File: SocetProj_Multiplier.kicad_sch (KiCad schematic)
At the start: 23 parts, among them J1 Barrel_Jack, U1 74LS283, U2 74LS283, U4 74LS86, U5 74LS86

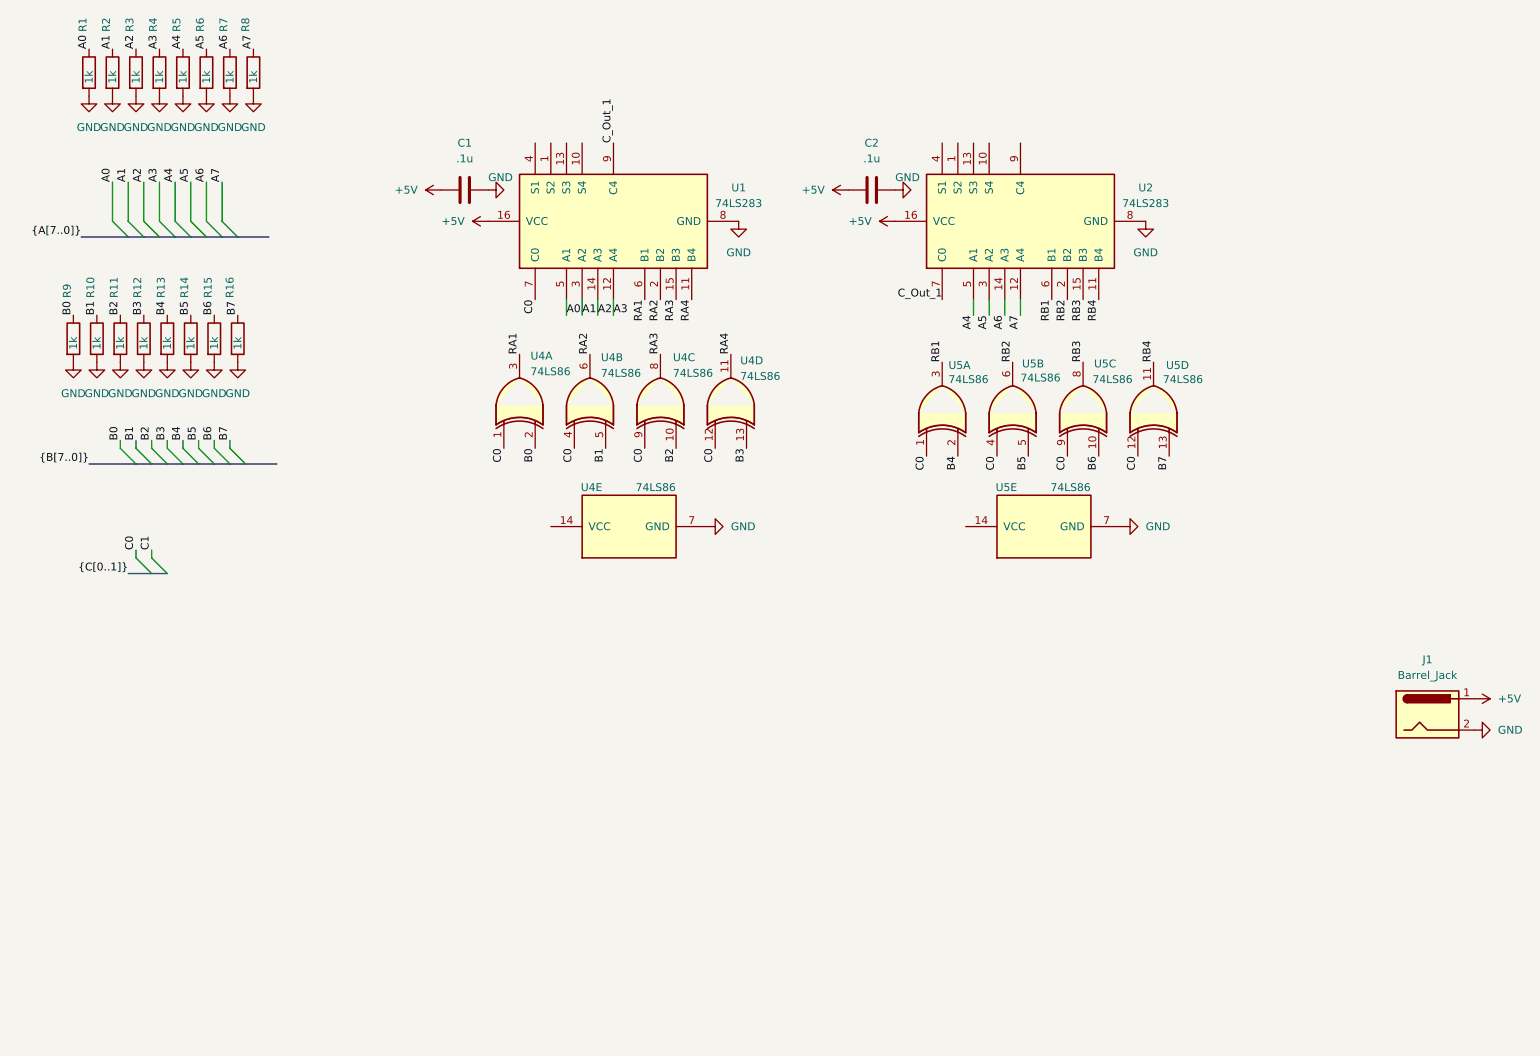
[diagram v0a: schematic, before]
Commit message: Begun Dadda logic
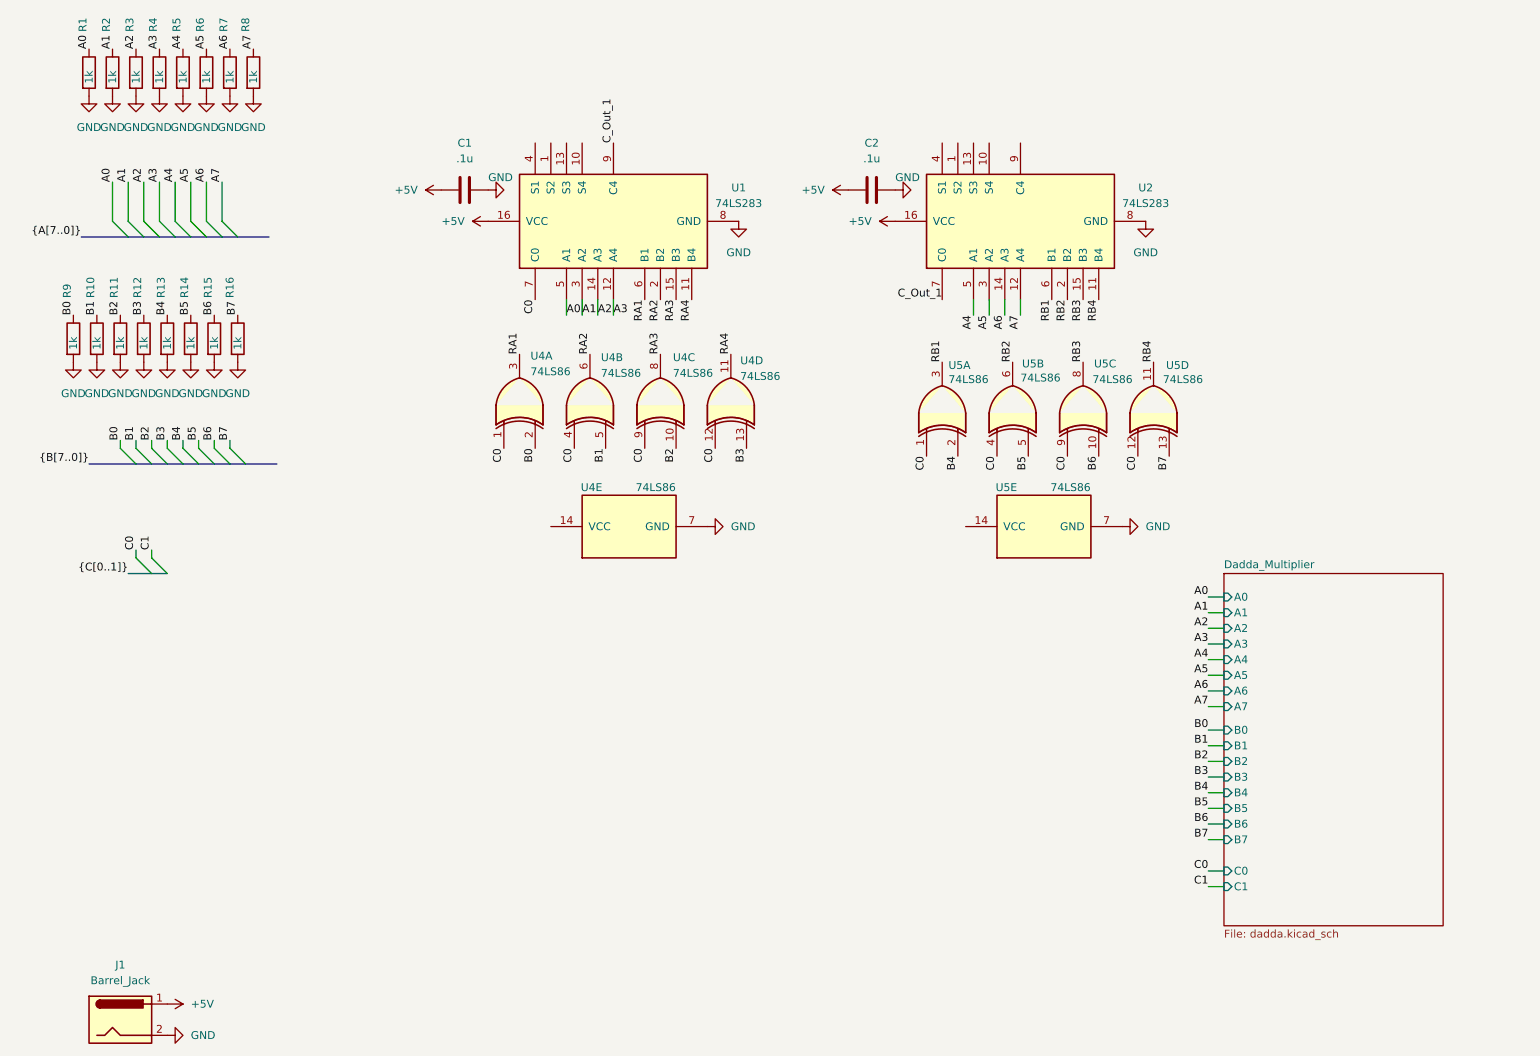
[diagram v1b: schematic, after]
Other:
- added sheet Dadda_Multiplier (dadda.kicad_sch)
- moved on the sheet: J1

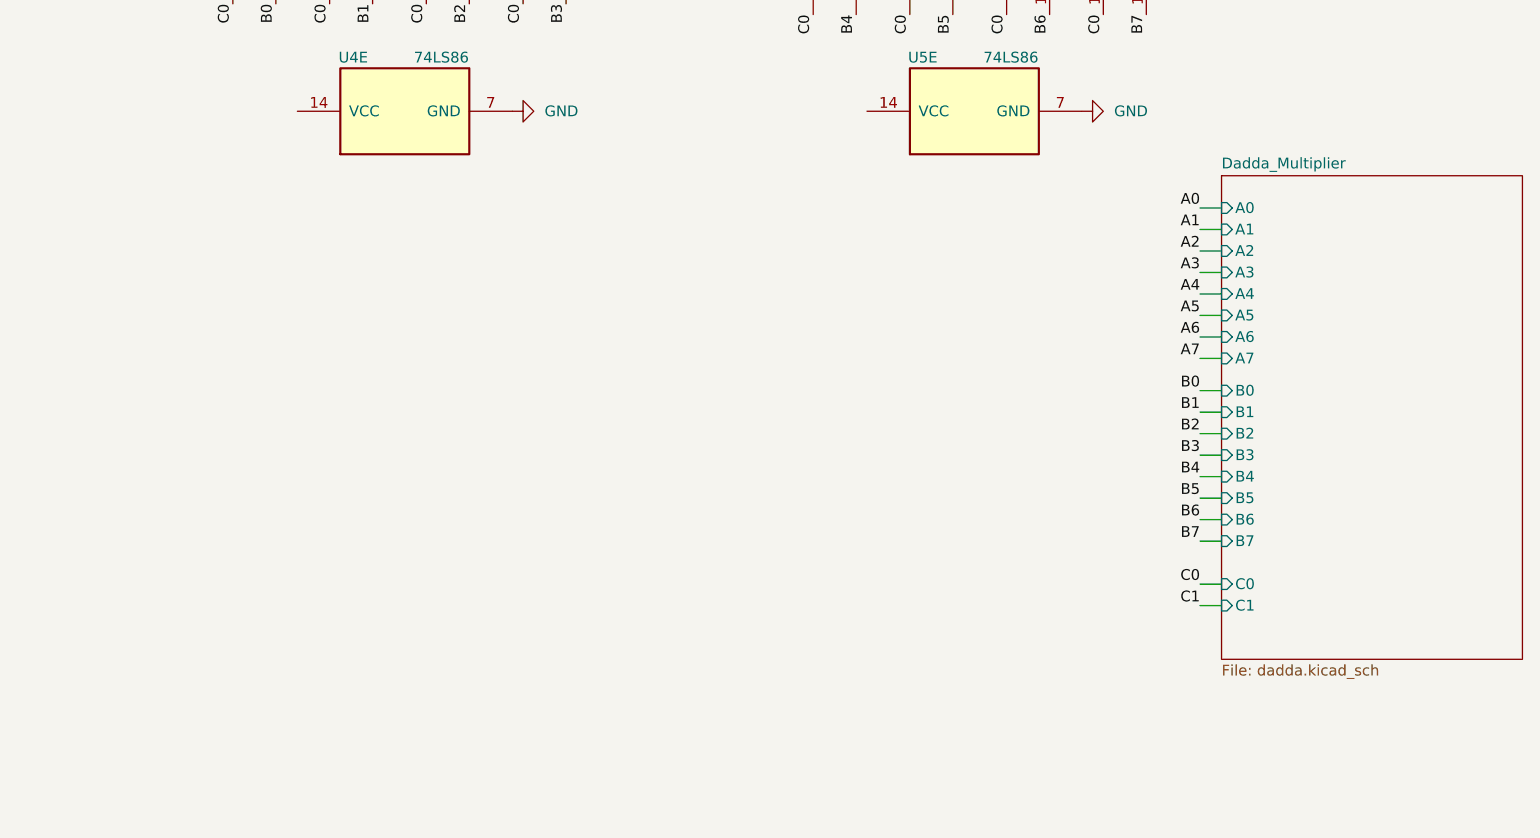
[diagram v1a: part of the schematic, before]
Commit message: Added hierarchal partial product outputs, need to complete treemultiplier
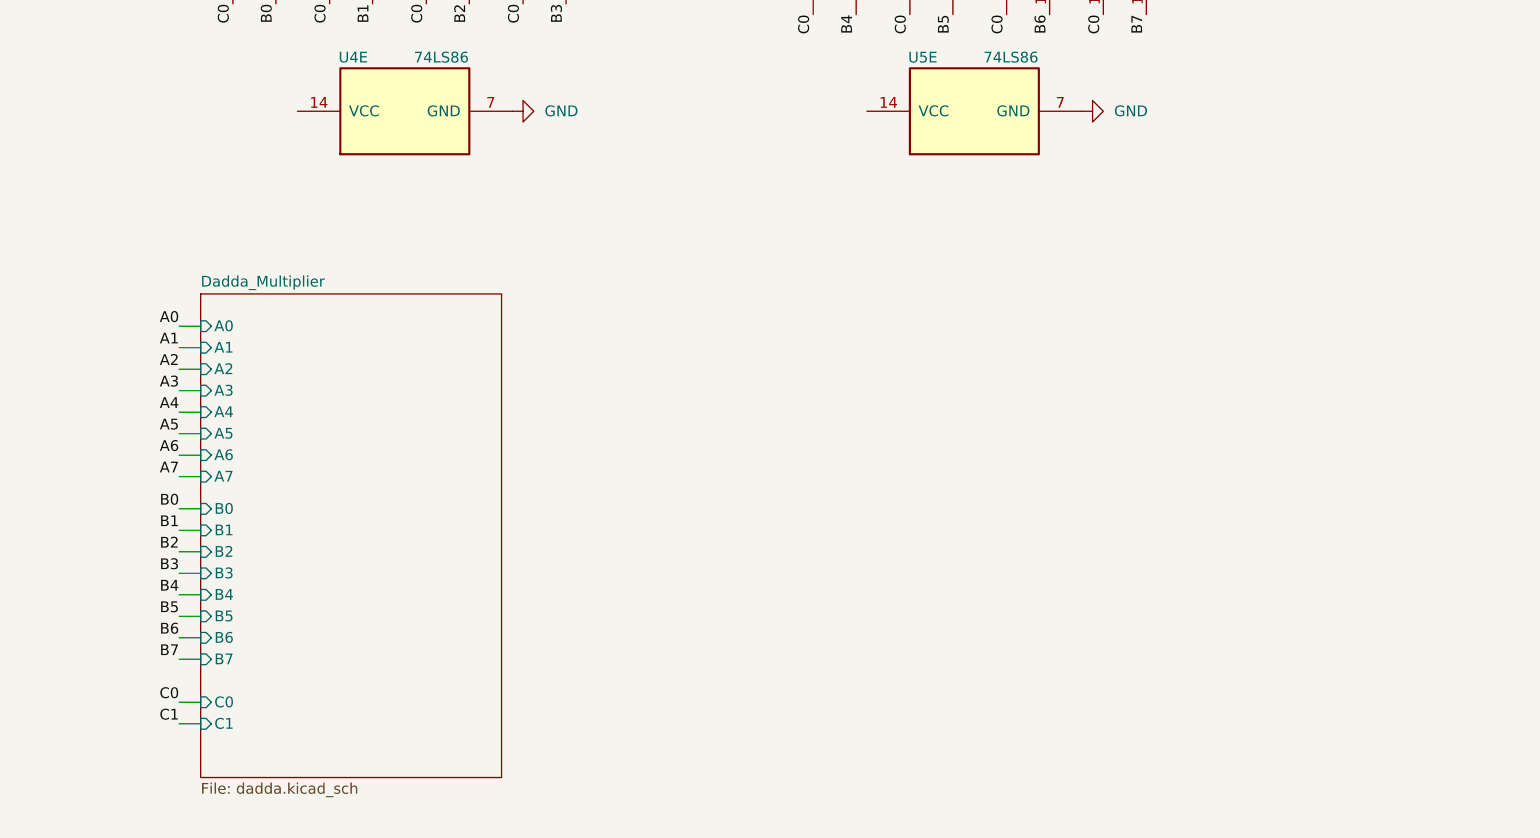
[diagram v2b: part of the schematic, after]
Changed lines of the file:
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@@
 	(wire
 		(pts
-			(xy 213.36 116.84) (xy 215.9 116.84)
+			(xy 92.71 130.81) (xy 95.25 130.81)
 		)
 		(stroke
@@
 	(wire
 		(pts
-			(xy 213.36 121.92) (xy 215.9 121.92)
+			(xy 92.71 135.89) (xy 95.25 135.89)
 		)
 		(stroke
@@
 	(wire
 		(pts
-			(xy 213.36 127) (xy 215.9 127)
+			(xy 92.71 140.97) (xy 95.25 140.97)
 		)
 		(stroke
@@
 	(wire
 		(pts
-			(xy 213.36 124.46) (xy 215.9 124.46)
+			(xy 92.71 138.43) (xy 95.25 138.43)
 		)
 		(stroke
@@
 	(wire
 		(pts
-			(xy 213.36 135.89) (xy 215.9 135.89)
+			(xy 92.71 149.86) (xy 95.25 149.86)
 		)
 		(stroke
@@
 	(wire
 		(pts
-			(xy 213.36 114.3) (xy 215.9 114.3)
+			(xy 92.71 128.27) (xy 95.25 128.27)
 		)
 		(stroke
@@
 	(wire
 		(pts
-			(xy 213.36 153.67) (xy 215.9 153.67)
+			(xy 92.71 167.64) (xy 95.25 167.64)
 		)
 		(stroke
@@
 	(wire
 		(pts
-			(xy 213.36 119.38) (xy 215.9 119.38)
+			(xy 92.71 133.35) (xy 95.25 133.35)
 		)
 		(stroke
@@
 	(wire
 		(pts
-			(xy 213.36 111.76) (xy 215.9 111.76)
+			(xy 92.71 125.73) (xy 95.25 125.73)
 		)
 		(stroke
@@
 	(wire
 		(pts
-			(xy 213.36 133.35) (xy 215.9 133.35)
+			(xy 92.71 147.32) (xy 95.25 147.32)
 		)
 		(stroke
@@
 	(wire
 		(pts
-			(xy 213.36 156.21) (xy 215.9 156.21)
+			(xy 92.71 170.18) (xy 95.25 170.18)
 		)
 		(stroke
@@
 	(wire
 		(pts
-			(xy 213.36 138.43) (xy 215.9 138.43)
+			(xy 92.71 152.4) (xy 95.25 152.4)
 		)
 		(stroke
@@
 	(wire
 		(pts
-			(xy 213.36 109.22) (xy 215.9 109.22)
+			(xy 92.71 123.19) (xy 95.25 123.19)
 		)
 		(stroke
@@
 	(wire
 		(pts
-			(xy 213.36 146.05) (xy 215.9 146.05)
+			(xy 92.71 160.02) (xy 95.25 160.02)
 		)
 		(stroke
@@
 	(wire
 		(pts
-			(xy 213.36 148.59) (xy 215.9 148.59)
+			(xy 92.71 162.56) (xy 95.25 162.56)
 		)
 		(stroke
@@
 	(wire
 		(pts
-			(xy 213.36 143.51) (xy 215.9 143.51)
+			(xy 92.71 157.48) (xy 95.25 157.48)
 		)
 		(stroke
@@
 	(wire
 		(pts
-			(xy 213.36 130.81) (xy 215.9 130.81)
+			(xy 92.71 144.78) (xy 95.25 144.78)
 		)
 		(stroke
@@
 	(wire
 		(pts
-			(xy 213.36 140.97) (xy 215.9 140.97)
+			(xy 92.71 154.94) (xy 95.25 154.94)
 		)
 		(stroke
@@
 	)
 	(label "B0"
-		(at 213.36 130.81 180)
+		(at 92.71 144.78 180)
 		(effects
 			(font
@@
 	)
 	(label "A6"
-		(at 213.36 124.46 180)
+		(at 92.71 138.43 180)
 		(effects
 			(font
@@
 	)
 	(label "A7"
-		(at 213.36 127 180)
+		(at 92.71 140.97 180)
 		(effects
 			(font
@@
 	)
 	(label "A2"
-		(at 213.36 114.3 180)
+		(at 92.71 128.27 180)
 		(effects
 			(font
@@
 	)
 	(label "B1"
-		(at 213.36 133.35 180)
+		(at 92.71 147.32 180)
 		(effects
 			(font
@@
 	)
 	(label "A1"
-		(at 213.36 111.76 180)
+		(at 92.71 125.73 180)
 		(effects
 			(font
@@
 	)
 	(label "B2"
-		(at 213.36 135.89 180)
+		(at 92.71 149.86 180)
 		(effects
 			(font
@@
 	)
 	(label "A0"
-		(at 213.36 109.22 180)
+		(at 92.71 123.19 180)
 		(effects
 			(font
@@
 	)
 	(label "B7"
-		(at 213.36 148.59 180)
+		(at 92.71 162.56 180)
 		(effects
 			(font
@@
 	)
 	(label "B6"
-		(at 213.36 146.05 180)
+		(at 92.71 160.02 180)
 		(effects
 			(font
@@
 	)
 	(label "B5"
-		(at 213.36 143.51 180)
+		(at 92.71 157.48 180)
 		(effects
 			(font
@@
 	)
 	(label "A4"
-		(at 213.36 119.38 180)
+		(at 92.71 133.35 180)
 		(effects
 			(font
@@
 	)
 	(label "C0"
-		(at 213.36 153.67 180)
+		(at 92.71 167.64 180)
 		(effects
 			(font
@@
 	)
 	(label "B4"
-		(at 213.36 140.97 180)
+		(at 92.71 154.94 180)
 		(effects
 			(font
@@
 	)
 	(label "B3"
-		(at 213.36 138.43 180)
+		(at 92.71 152.4 180)
 		(effects
 			(font
@@
 	)
 	(label "C1"
-		(at 213.36 156.21 180)
+		(at 92.71 170.18 180)
 		(effects
 			(font
@@
 	)
 	(label "A3"
-		(at 213.36 116.84 180)
+		(at 92.71 130.81 180)
 		(effects
 			(font
@@
 	)
 	(label "A5"
-		(at 213.36 121.92 180)
+		(at 92.71 135.89 180)
 		(effects
 			(font
@@
 	)
 	(sheet
-		(at 215.9 105.41)
+		(at 95.25 119.38)
 		(size 35.56 57.15)
 		(exclude_from_sim no)
@@
 		)
 		(property "Sheetname" "Dadda_Multiplier"
-			(at 215.9 104.6984 0)
+			(at 95.25 118.6684 0)
 			(effects
 				(font
@@
 		)
 		(property "Sheetfile" "dadda.kicad_sch"
-			(at 215.9 163.1446 0)
+			(at 95.25 177.1146 0)
 			(effects
 				(font
@@
 		)
 		(pin "A0" input
-			(at 215.9 109.22 180)
+			(at 95.25 123.19 180)
 			(effects
 				(font
@@
 		)
 		(pin "A1" input
-			(at 215.9 111.76 180)
+			(at 95.25 125.73 180)
 			(effects
 				(font
@@
 		)
 		(pin "A2" input
-			(at 215.9 114.3 180)
+			(at 95.25 128.27 180)
 			(effects
 				(font
@@
 		)
 		(pin "A3" input
-			(at 215.9 116.84 180)
+			(at 95.25 130.81 180)
 			(effects
 				(font
@@
 		)
 		(pin "A4" input
-			(at 215.9 119.38 180)
+			(at 95.25 133.35 180)
 			(effects
 				(font
@@
 		)
 		(pin "A5" input
-			(at 215.9 121.92 180)
+			(at 95.25 135.89 180)
 			(effects
 				(font
@@
 		)
 		(pin "A6" input
-			(at 215.9 124.46 180)
+			(at 95.25 138.43 180)
 			(effects
 				(font
@@
 		)
 		(pin "A7" input
-			(at 215.9 127 180)
+			(at 95.25 140.97 180)
 			(effects
 				(font
@@
 		)
 		(pin "B0" input
-			(at 215.9 130.81 180)
+			(at 95.25 144.78 180)
 			(effects
 				(font
@@
 		)
 		(pin "B1" input
-			(at 215.9 133.35 180)
+			(at 95.25 147.32 180)
 			(effects
 				(font
@@
 		)
 		(pin "B2" input
-			(at 215.9 135.89 180)
+			(at 95.25 149.86 180)
 			(effects
 				(font
@@
 		)
 		(pin "B3" input
-			(at 215.9 138.43 180)
+			(at 95.25 152.4 180)
 			(effects
 				(font
@@
 		)
 		(pin "B4" input
-			(at 215.9 140.97 180)
+			(at 95.25 154.94 180)
 			(effects
 				(font
@@
 		)
 		(pin "B5" input
-			(at 215.9 143.51 180)
+			(at 95.25 157.48 180)
 			(effects
 				(font
@@
 		)
 		(pin "B6" input
-			(at 215.9 146.05 180)
+			(at 95.25 160.02 180)
 			(effects
 				(font
@@
 		)
 		(pin "B7" input
-			(at 215.9 148.59 180)
+			(at 95.25 162.56 180)
 			(effects
 				(font
@@
 		)
 		(pin "C0" input
-			(at 215.9 153.67 180)
+			(at 95.25 167.64 180)
 			(effects
 				(font
@@
 		)
 		(pin "C1" input
-			(at 215.9 156.21 180)
+			(at 95.25 170.18 180)
 			(effects
 				(font
